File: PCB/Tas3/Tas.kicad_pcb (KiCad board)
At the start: 2 copper layers, 70 x 70 mm, 36 parts, among them J1 Shelly 1, J2 Conn_01x07, J3 USB-C, Q1 PMF170XP,115, Q2 2N7002BKS, U1 MD8942, U2 Barcode, U3 CH340X

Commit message: Better rails
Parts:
- removed FID1, FID2, FID3, FID4, FID5, FID6, FID7, FID8: Fiducial, Fiducial:Fiducial_1mm_Mask2mm
- added PCB1: 70x70, RevK:PCB7070, F.Cu at (135.0, 65.0)
- moved U2 3.55 mm to (153.4, 68.3)
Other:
- outline, holes or cut-outs redrawn
- board text added: "2 Designs, 0.8mm, Black"
- board text removed: "2 Designs, 0.8mm, Black, V-Cuts"

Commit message: Revised totally
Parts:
- removed D2: BAV99S, RevK:SOT-363_SC-70-6
- removed Q1: PMF170XP,115, RevK:SOT-323_SC-70
- removed Q2: 2N7002BKS, RevK:SOT-363_SC-70-6
- removed R9: 10k, RevK:R_0402
- added U4: ISL89410, RevK:SO-8_3.9x4.9mm_P1.27mm, F.Cu at (136.0, 45.4)
- moved D1 0.20 mm to (139.1, 55.0)
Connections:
- D1 pad 3: RST -> R
- J1 pad 2: GPIO0 -> B
- J1 pad 3: B -> RST+
- J2 pad 2: GPIO0 -> B
- J2 pad 3: B -> RST+
- R8 pad 2: +3V3 -> Net-(U3-~{CTS})
- U3 pad 5: GND -> Net-(U3-~{CTS})
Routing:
- net RST+: track 0.00 -> 8.58 mm
- net GPIO0: track 14.9 -> 8.73 mm, vias 1 -> 2
- net Net-(Q1-G): track 6.06 -> 0.00 mm
- net R: track 32.0 -> 36.9 mm
- net RST: track 25.2 -> 20.4 mm
- net Net-(U3-~{CTS}): track 0.00 -> 3.85 mm
- net GND: track 14.6 -> 10.8 mm, vias 8 -> 12
- net +3V3: track 40.6 -> 39.3 mm, vias 2 -> 0
- net VBUS: track 21.6 -> 21.1 mm

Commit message: VCUT
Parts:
- added V1: ~, RevK:VCUT70, F.Cu at (100.0, 68.9)
- added V2: ~, RevK:VCUT70, F.Cu at (100.0, 40.6)
- moved U2 36.0 mm to (117.5, 71.3)
- moved C5 35.1 mm to (94.3, 50.5)
- moved D5 35.1 mm to (94.3, 45.2)
- moved J2 35.1 mm to (100.7, 44.6)
- moved R10 35.1 mm to (93.8, 52.0)
- moved R11 35.1 mm to (94.3, 47.0)
- moved Art1 35.1 mm to (96.5, 56.6)
- moved Art2 35.1 mm to (99.0, 66.0)
- moved C1 35.1 mm to (93.6, 54.1)
- moved C6 35.1 mm to (98.6, 54.1)
- moved C7 35.1 mm to (96.1, 54.8)
- moved D1 35.1 mm to (104.1, 58.0)
- moved J1 35.1 mm to (99.0, 42.1)
- moved J3 35.1 mm to (99.0, 64.5)
- moved L2 35.1 mm to (96.1, 57.4)
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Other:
- board text added: "${TITLE}"
- board text removed: "2 Designs, 0.8mm, Black"
- board text removed: "PCB-TAS"

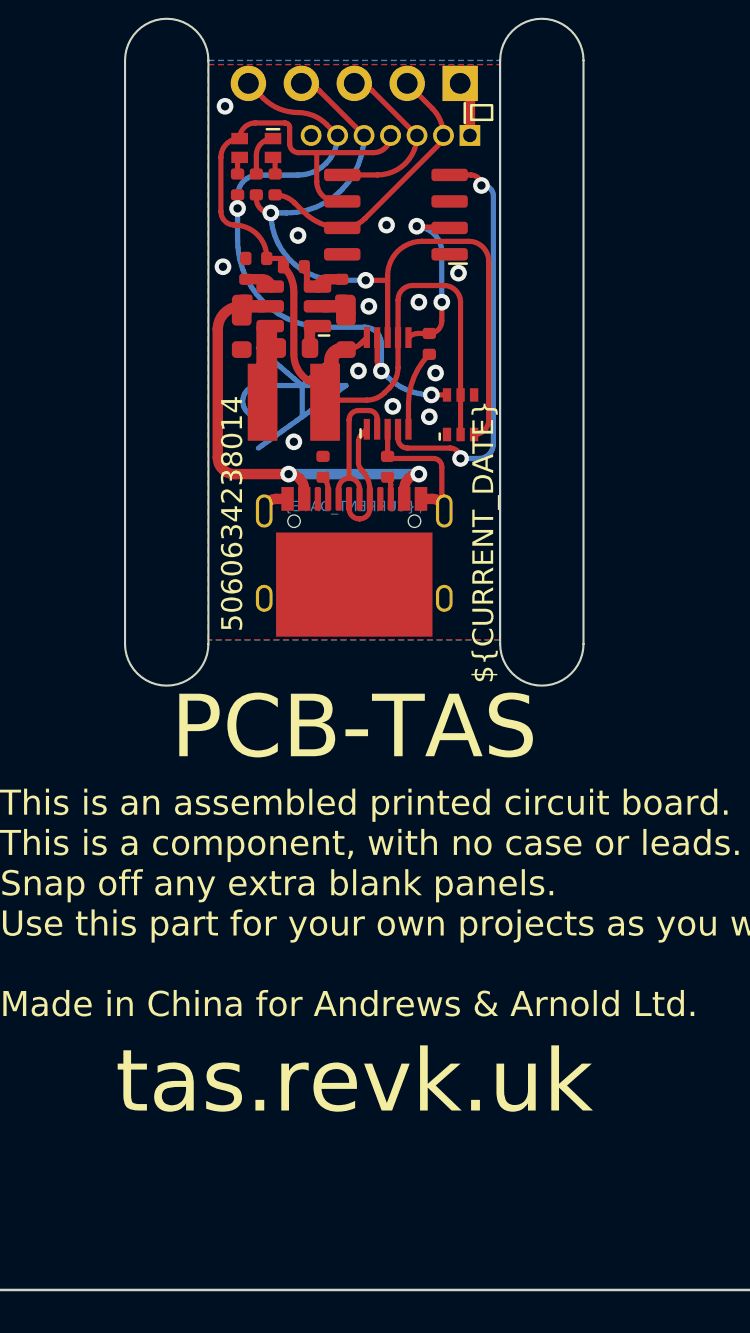
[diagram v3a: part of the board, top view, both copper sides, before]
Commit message: Swapped connector to top for single sided assembly
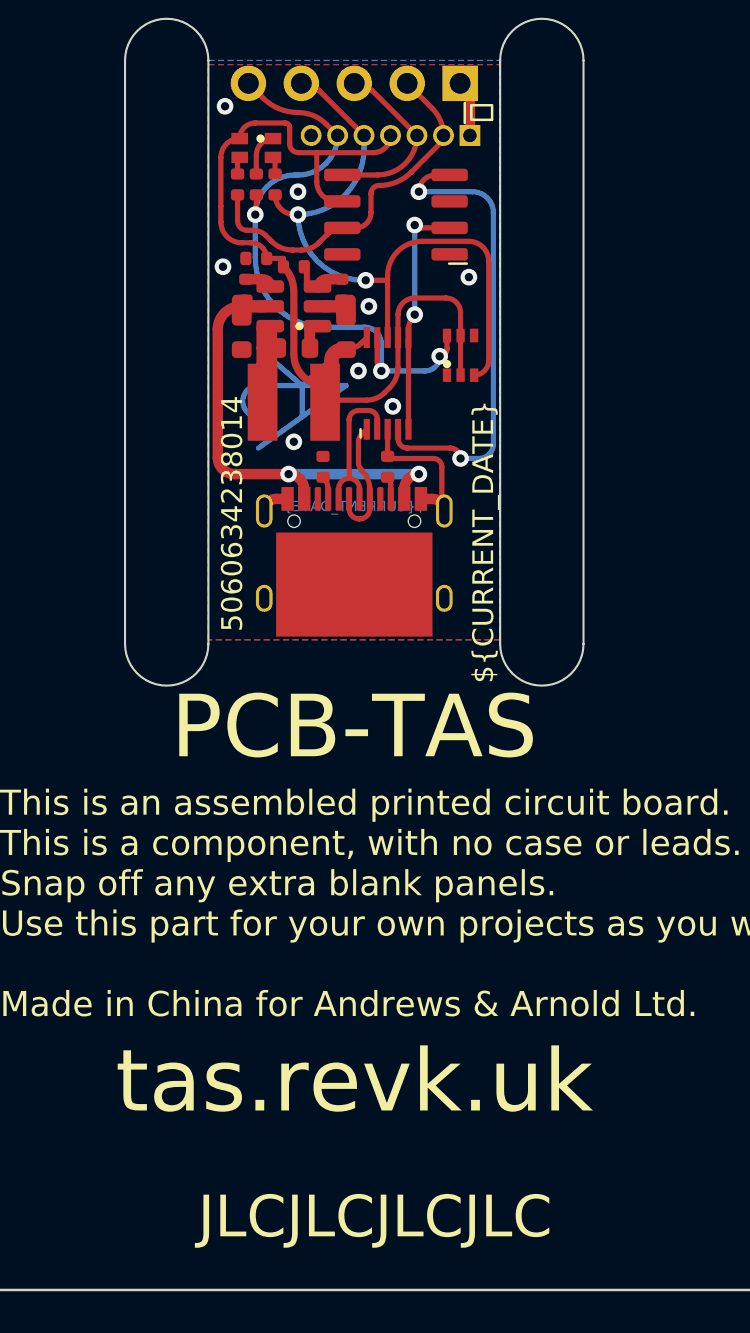
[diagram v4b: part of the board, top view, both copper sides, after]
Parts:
- removed R8: 4k7, RevK:R_0402
- J2: moved to F.Cu
- moved D1 2.85 mm to (104.1, 55.1)
- moved R12 1.80 mm to (95.2, 47.0)
- moved R13 1.80 mm to (93.4, 47.0)
- turned J2 to -90 degrees
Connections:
- D1 pad 3: R -> G
- D1 pad 6: G -> R
- D5 pad 2: Net-(D5-BK) -> Net-(D5-GK)
- D5 pad 3: Net-(D5-GK) -> Net-(D5-BK)
- J1 pad 4: R -> G
- J1 pad 5: G -> R
- J2 pad 5: R -> G
- J2 pad 6: G -> R
- U3 pad 5: Net-(U3-~{CTS}) -> GPIO0
- U3 pad 8: R -> G
- U3 pad 9: G -> R
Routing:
- net R: track 36.9 -> 29.7 mm, vias 2 -> 3
- net Net-(U3-~{CTS}): track 3.85 -> 0.00 mm
- net +3V3: track 39.3 -> 35.5 mm
- net B: track 13.5 -> 17.0 mm
- net GPIO0: track 8.73 -> 11.2 mm
- net RST: track 20.4 -> 22.3 mm
- net G: track 30.2 -> 32.1 mm, vias 3 -> 2
- net GND: vias 12 -> 8
